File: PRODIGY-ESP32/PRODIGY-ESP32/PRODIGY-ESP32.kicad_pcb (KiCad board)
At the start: 2 copper layers, 22 x 42 mm, 17 parts, among them J1 Bus_M.2_Socket_B, Q1 BC850, Q2 BC850, SW1 SW_Push, U1 ESP32-S3-WROOM-1, U2 FT231XQ, U3 TS3USB221AQRSERQ1

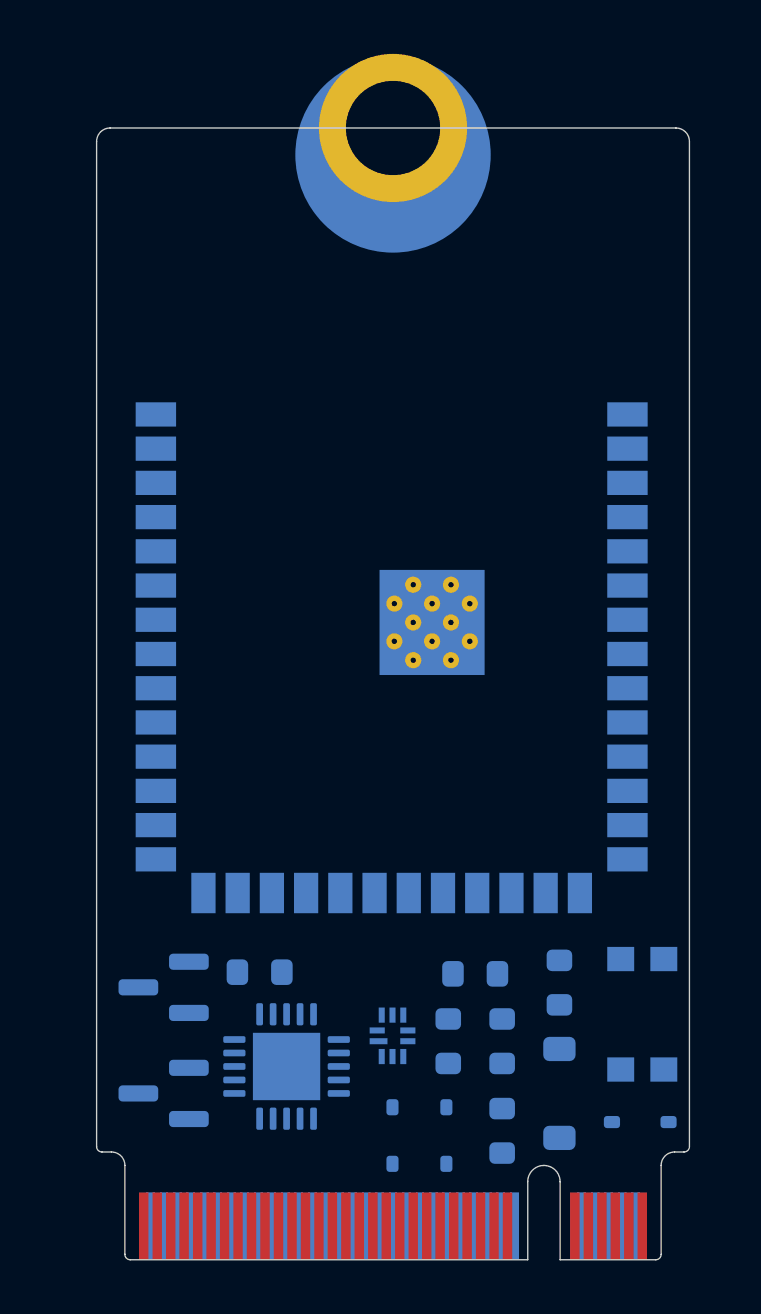
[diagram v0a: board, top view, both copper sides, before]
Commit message: All footprint assosiations have been made across all schematics.
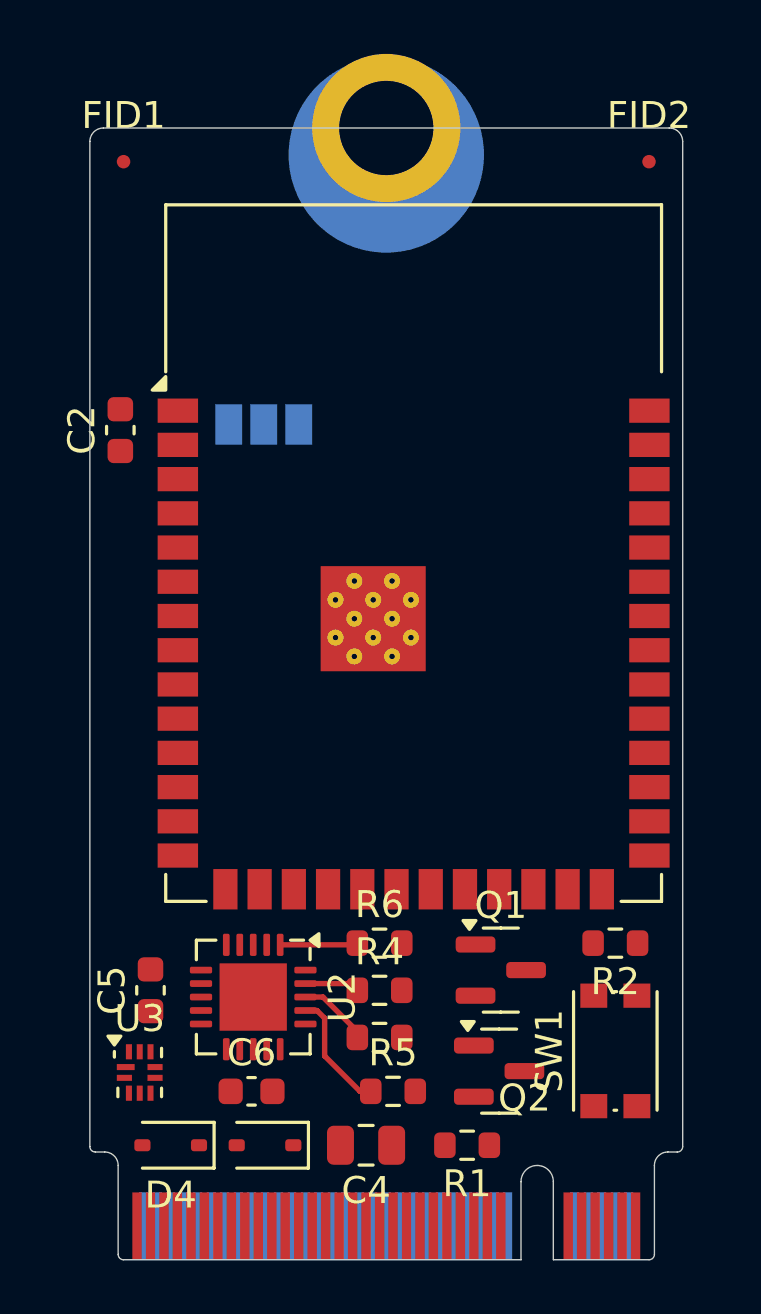
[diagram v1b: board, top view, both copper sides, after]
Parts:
- removed D1: SD05_SOD323, Diode_SMD:D_SOD-323
- removed D2: 1N4148W, Diode_SMD:D_SOD-123
- added C2: 100nF, Capacitor_SMD:C_0603_1608Metric, F.Cu at (170.6, 73.5)
- added C4: 10uF, Capacitor_SMD:C_0805_2012Metric, F.Cu at (179.8, 100.0)
- added C5: 100nF, Capacitor_SMD:C_0603_1608Metric, F.Cu at (171.8, 94.2)
- added C6: 100nF, Capacitor_SMD:C_0603_1608Metric, F.Cu at (175.5, 98.0)
- added FID1: Fiducial, Fiducial:Fiducial_0.5mm_Mask1.5mm, F.Cu at (170.8, 63.5)
- added FID2: Fiducial, Fiducial:Fiducial_0.5mm_Mask1.5mm, F.Cu at (190.2, 63.5)
- added JP1: Jumper_3_Bridged12, Jumper:SolderJumper-3_P1.3mm_Open_Pad1.0x1.5mm, B.Cu at (175.9, 73.2)
- D3, D4, Q1, Q2, R1, R3, R4, R5, R6, SW1, U1, U2, U3: moved to F.Cu
- R2: value 10k -> 1k; moved to F.Cu
- moved D4 17.4 mm to (172.5, 100.0)
- moved Q1 12.5 mm to (184.8, 93.5), turned to 0 degrees
- moved Q2 12.5 mm to (184.7, 97.2), turned to 0 degrees
- moved R1 10.0 mm to (183.5, 100.0)
- moved U3 9.48 mm to (171.3, 97.3)
- moved R3 5.72 mm to (180.2, 96.0), turned to 0 degrees
- moved D3 4.74 mm to (176.0, 100.0), turned to 180 degrees
- moved R5 4.46 mm to (180.8, 98.0), turned to 0 degrees
- moved R6 3.73 mm to (180.2, 92.5)
- moved R4 3.17 mm to (180.2, 94.2), turned to 0 degrees
- moved U2 2.86 mm to (175.6, 94.5), turned to -90 degrees
- moved R2 2.54 mm to (189.0, 92.5), turned to 180 degrees
- moved SW1 1.69 mm to (189.0, 96.5)
- moved U1 0.83 mm to (181.5, 78.0), turned to 0 degrees
- moved J1 0.25 mm to (180.5, 104.2)
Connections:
- J1 pad P$7: /USB_D+ -> (no net)
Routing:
- net Net-(U2-TXD): track 0.00 -> 4.49 mm
- net Net-(U2-RXD): track 0.00 -> 2.89 mm
- net /DTR: track 0.00 -> 2.68 mm
- net /RTS: track 0.00 -> 2.03 mm

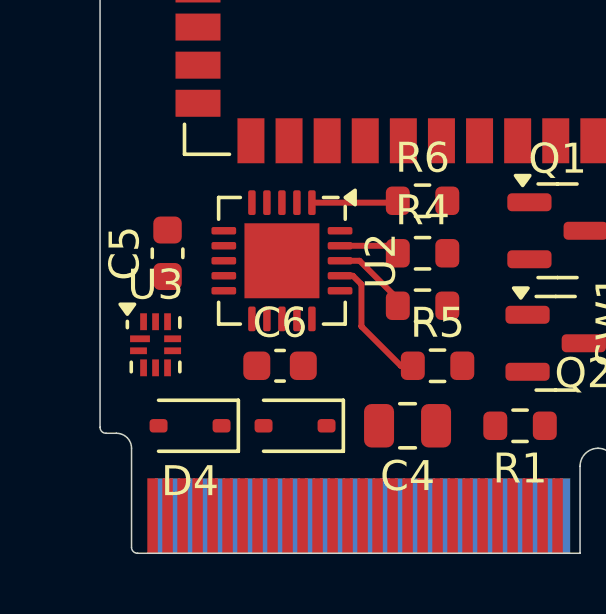
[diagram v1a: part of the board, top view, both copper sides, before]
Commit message: ESP32 and ATMEGA bom done.
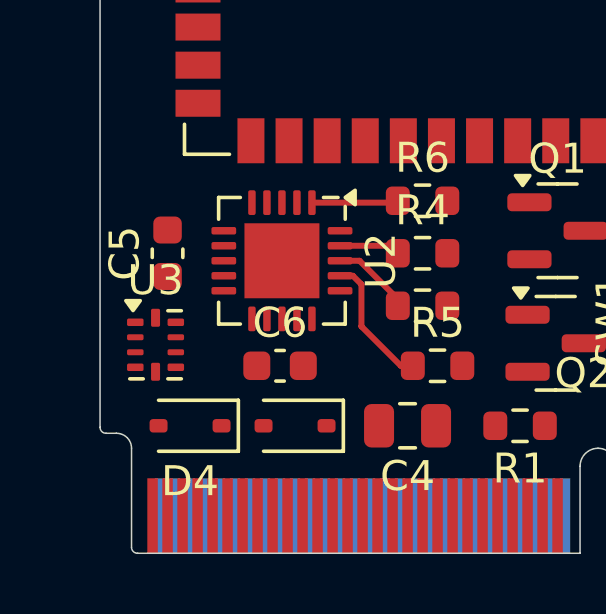
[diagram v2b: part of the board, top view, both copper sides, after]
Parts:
- U3: footprint Package_DFN_QFN:UQFN-10_1.4x1.8mm_P0.4mm -> Package_DFN_QFN:Texas_UQFN-10_1.5x2mm_P0.5mm

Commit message: Shcematic fixes to ESP32
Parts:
- removed C5, C6: 100nF, Capacitor_SMD:C_0603_1608Metric
- removed D3, D4: SD05_SOD323, Diode_SMD:D_SOD-323
- added C1: 10uF, Capacitor_SMD:C_0805_2012Metric, F.Cu at (179.9, 100.0)
- added C3: 100nF, Capacitor_SMD:C_0603_1608Metric, F.Cu at (178.0, 98.0)
- added D1: SD05_SOD323, Diode_SMD:D_SOD-323, F.Cu at (176.2, 100.0)
- added D2: SD05_SOD323, Diode_SMD:D_SOD-323, F.Cu at (172.8, 100.0)
- C4: value 10uF -> 100nF; footprint Capacitor_SMD:C_0805_2012Metric -> Capacitor_SMD:C_0603_1608Metric
- JP1: moved to F.Cu
- R2: value 1k -> 10k
- R4: value 10k -> 1k
- U2: value FT231XQ -> TS3USB221AQRSERQ1; footprint Package_DFN_QFN:QFN-20-1EP_4x4mm_P0.5mm_EP2.5x2.5mm -> Package_DFN_QFN:Texas_UQFN-10_1.5x2mm_P0.5mm
- U3: value TS3USB221AQRSERQ1 -> FT231XQ; footprint Package_DFN_QFN:Texas_UQFN-10_1.5x2mm_P0.5mm -> Package_DFN_QFN:QFN-20-1EP_4x4mm_P0.5mm_EP2.5x2.5mm
- moved R4 8.92 mm to (189.0, 92.5), turned to 180 degrees
- moved R2 8.61 mm to (181.2, 96.2), turned to 0 degrees
- moved JP1 7.90 mm to (170.8, 79.2), turned to -90 degrees
- moved C4 5.39 mm to (174.8, 98.0), turned to 0 degrees
- moved U3 5.27 mm to (175.8, 94.5), turned to -90 degrees
- moved U2 4.32 mm to (171.2, 94.8), turned to 180 degrees
- moved R3 1.80 mm to (181.2, 94.5)
- moved R6 1.03 mm to (181.2, 92.8)
- moved R5 0.50 mm to (181.2, 98.0)
- moved C2 0.43 mm to (171.0, 73.2)
- moved Q1 0.25 mm to (185.0, 93.5)
- moved Q2 0.25 mm to (184.9, 97.2)
- moved SW1 0.25 mm to (189.0, 96.2)
- moved U1 0.24 mm to (181.8, 78.0)
- moved R1 0.05 mm to (183.4, 100.0)
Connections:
- JP1 pad 1: GND -> +3V3
- JP1 pad 3: +3V3 -> GND
- R2 pad 1: Net-(R1-Pad1) -> /DTR
- R2 pad 2: /ESP_BUTTON_BOOT -> Net-(Q1-B)
- R3 pad 1: /DTR -> /RTS
- R3 pad 2: Net-(Q1-B) -> Net-(Q2-B)
- R4 pad 1: /RTS -> Net-(R1-Pad1)
- R4 pad 2: Net-(Q2-B) -> /ESP_BUTTON_BOOT
- R5 pad 1: Net-(U2-TXD) -> Net-(U3-TXD)
- R6 pad 1: Net-(U2-RXD) -> Net-(U3-RXD)
- U1 pad 13: /USB_D1- -> /USB_D2-
- U1 pad 14: /USB_D1+ -> /USB_D2+
- U2 pad 1: Net-(U2-RXD) -> /USB_D1+
- U2 pad 2: unconnected-(U2-~{RI}-Pad2) -> /USB_D1-
- U2 pad 3: GND -> /USB_D2+
- U2 pad 4: unconnected-(U2-~{DSR}-Pad4) -> /USB_D2-
- U2 pad 5: unconnected-(U2-~{DCD}-Pad5) -> GND
- U2 pad 6: unconnected-(U2-~{CTS}-Pad6) -> GND
- U2 pad 7: unconnected-(U2-CBUS2-Pad7) -> /USB_D-
- U2 pad 8: /USB_D2+ -> /USB_D+
- U2 pad 9: /USB_D2- -> Net-(JP1-C)
- U3 pad 1: /USB_D1+ -> Net-(U3-RXD)
- U3 pad 10: Net-(JP1-C) -> +3V3
- U3 pad 2: /USB_D2+ -> unconnected-(U3-~{RI}-Pad2)
- U3 pad 3: /USB_D+ -> GND
- U3 pad 4: GND -> unconnected-(U3-~{DSR}-Pad4)
- U3 pad 5: /USB_D- -> unconnected-(U3-~{DCD}-Pad5)
- U3 pad 6: /USB_D2- -> unconnected-(U3-~{CTS}-Pad6)
- U3 pad 7: /USB_D1- -> unconnected-(U3-CBUS2-Pad7)
- U3 pad 8: GND -> /USB_D1+
- U3 pad 9: +3V3 -> /USB_D1-
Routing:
- net Net-(U2-TXD): track 4.49 -> 0.00 mm
- net Net-(U2-RXD): track 2.89 -> 0.00 mm
- net /DTR: track 2.68 -> 0.00 mm
- net /RTS: track 2.03 -> 0.00 mm
